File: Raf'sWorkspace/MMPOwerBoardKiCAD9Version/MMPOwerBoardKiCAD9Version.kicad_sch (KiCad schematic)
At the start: 31 parts, among them J1 TYPE-C-31-M-04, J2 Conn_02x16_Odd_Even, U1 HUSB237, U10 TPS22917DBVR, U2 TP4056-42-ESOP8, U3 DRV8833PWPR, U4 TPS63802DLAR, U5 TPS22917DBVR, U6 TPS61235PRWLR, U7 INA219AIDR, U8 TPS62133RGTR, U9 DRV8833PWPR

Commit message: Added a few things to schematic and added new LDO schematic to library
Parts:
- added C10, C11, C12, C14: 22u, symbol Device:C
- added C13, C8: 10u, symbol Device:C
- added C9: 1u, symbol Device:C
- added L1: 1uH, symbol Device:L
- added L2: 47uH, symbol Device:L
- added R12: 1M, symbol Device:R_Small_US
- added R13: 332k, symbol Device:R_Small_US
- added R14: 511k, symbol Device:R_Small_US
- added R15: 91k, symbol Device:R_Small_US
- added R16: 100k, symbol Device:R_Small_US
- added R17, R18: 4.7k, symbol Device:R_Small_US
- added U11: AMS1117-5.0, symbol AMS1117-CUSTOM5V:AMS1117-5.0
- U6: value TPS61235PRWLR -> TPS61236PRWLR
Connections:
- net 5V_OUT is gone; now on net 5V: J2.20 (Pin_20)
- net 3V3: now also U4.6 (VOUT), C14.1, R14.1
- net EXT_LOAD1_CTRL: now also U5.3 (ON), R17.1
- net EXT_LOAD1_OUT: now also U5.6 (VOUT)
- net EXT_LOAD2_CTRL: now also U10.3 (ON), R18.1
- net EXT_LOAD2_OUT: now also U10.6 (VOUT)
- net FromBattery: now also U4.1 (EN), U4.10 (VIN), U6.3 (VIN), U6.7 (EN), C13.1, C8.1, C9.1, L1.1, R16.1
- net GND: now also U10.2 (GND), U4.2 (MODE), U4.8 (GND), U5.2 (GND), U6.1 (PGND), C10.2, C11.2, C12.2, C13.2, C14.2, C8.2, C9.2, R17.2, R18.2
- net 5V: now reaches U5.1 (VIN)
- net 5V: now also U10.1 (VIN), U6.9 (VOUT), C10.1, C11.1, C12.1, R12.2
- net at U6.2 (SW): now also L1.2
- net GNDA: now reaches U6.4 (CC)
- net GNDA: now also U4.3 (AGND), U6.5 (AGND), U6.8 (INACT), R13.1, R15.2
- net at U6.6 (FB): now also R12.1, R13.2
- net at U4.4 (FB): now also R14.2, R15.1
- net at U4.5 (PG): now also R16.2
- net at U4.7 (L2): now also L2.1
- net at U4.9 (L1): now also L2.2
- no-connect marks 5 -> 9
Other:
- note added: "Make 0.whatever out of basic resistors"
- note added: "May wnat quick output discharge, only requires resistor but find out if worth it"
- note added: "STill need to get footprint from EASYEDA"
- moved on the sheet: C1, C2, C3, C4, C5, C6, C7, J1, R1, R10, R11, R2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

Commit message: Almost complete schematic
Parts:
- removed U8: TPS62133RGTR, TPS62133RGTR:QFN50P300X300X100-17N, symbol TPS62133RGTR:TPS62133RGTR
- added C15: 100n, symbol Device:C
- added C16: 1u, symbol Device:C
- added C18, C19: 22u, symbol Device:C
- added C20, C21: 10u, symbol Device:C
- added Q1: SS8050, Package_TO_SOT_SMD:SOT-23, symbol Transistor_BJT:SS8050
- added R19: 75k, symbol Device:R_Small_US
- added R20, R21, R22: 1M, symbol Device:R_Small_US
- added R23, R24: 1, symbol Device:R_Small_US
- added R25: 5.6k, symbol Device:R_Small_US
- added R26: 2.2k, symbol Device:R_Small_US
- added R27: 3.3k, symbol Device:R_Small_US
- U11: footprint (none) -> AMS1117_5.0_CUSTOM_FOOT:SOT-223_L6.5-W3.5-P2.30-LS7.0-BR
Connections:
- net HV is gone; now on net 9V: J2.22 (Pin_22)
- net 3V3: no longer C7.1, U7.1 (A1), U7.2 (A0), U7.5 (VS)
- net Battery: now also C7.1, U7.1 (A1), U7.2 (A0), U7.5 (VS)
- net ChargingCircuit: now also U2.5 (BAT), C21.1
- net FAST_CHARGE_CTRL: now also R27.1
- net FromBattery: no longer C13.1, C8.1, C9.1, L1.1, R16.1, U4.1 (EN), U4.10 (VIN), U6.3 (VIN), U6.7 (EN)
- net GND: now also J1.A1 (GND_A), J1.A12 (GND_A), J1.B1 (GND_B), J1.B12 (GND_B), U1.7 (GND), U11.1 (GND), U2.1 (TEMP), U2.3 (GND), U2.9 (EXP), C15.2, C16.2, C18.2, C19.2, C20.2, C21.2, Q1.2 (E), R19.2, R20.2, R21.2, R22.2, R25.1
- net LoadCircuit: now also C13.1, C8.1, C9.1, L1.1, R16.1, U4.1 (EN), U4.10 (VIN), U6.3 (VIN), U6.7 (EN)
- net at U11.2 (Vout): now also C19.1, R23.1, R24.1
- net 9V: now reaches U11.3 (Vin)
- net 9V: now also J1.A4 (VBUS_A), J1.A9 (VBUS_A), J1.B4 (VBUS_B), J1.B9 (VBUS_B), U1.2 (VUSB), C16.1, C18.1
- net at J1.A5 (CC1): now also U1.1 (CC1)
- net at J1.A6 (DP1): now also J1.B6 (DP2), U1.4 (D+)
- net at J1.A7 (DN1): now also J1.B7 (DN2), U1.5 (D-)
- net at J1.A8 (SUB1): now also R21.1
- net at J1.B5 (CC2): now also U1.6 (CC2)
- net at J1.B8 (SUB2): now also R22.1
- net at J1.S1 (SHIELD), J1.S2 (SHIELD), J1.S3 (SHIELD)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: now also C15.1, R20.1
- net at U2.2 (PROG): now also R25.2, R26.2
- net at U2.4 (VCC): now also U2.8 (CE), C20.1, R23.2, R24.2
- net at U1.3 (VSET): now also R19.1
- new net: Q1.3 (C), R26.1
- new net: Q1.1 (B), R27.2
- no-connect marks 9 -> 18
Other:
- note added: "Thermal Pad to GND, asks for via's, might be expensive... Current limiting ?"
- note removed: "STill need to get footprint from EASYEDA"
- note removed: "Thermal Pad to GND, asks for via's, might be expensive..."
- moved on the sheet: J1, U1, U11, U2

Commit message: Final Schematic complete with test points and jumpers
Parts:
- added D1, D2: LED, symbol Device:LED
- added JP1, JP2, JP3, JP4, JP5, JP6, JP7: SolderJumper_2_Open, symbol Jumper:SolderJumper_2_Open
- added L3: 22uH, symbol Device:L
- added R28, R29: 1k, symbol Device:R_Small_US
- added R30, R31, R32, R33: 0.1, symbol Device:R_Small_US
- added R34, R35, R37: 1, symbol Device:R_Small_US
- added R36: 2.2k, symbol Device:R_Small_US
- added TP1, TP10, TP11, TP12, TP13, TP14, TP15, TP16, TP17, TP18, TP19, TP2, TP3, TP4, TP5, TP6, TP7, TP8, TP9: TestPoint, symbol Connector:TestPoint
- L2: value 47uH -> 22uH
- R1, R2, R3, R4, R6, R7: footprint (none) -> Resistor_SMD:R_1206_3216Metric
- R13: value 332k -> 330k
- R14: value 511k -> 560k
- R15: value 91k -> 100k
- R5, R8: value 2 -> 1; footprint (none) -> Resistor_SMD:R_1206_3216Metric
- R9: value 0.4 -> 0.1
- SW1: footprint (none) -> SlideSwitch:SS-12D11-G050
- U1: footprint (none) -> HUSB237-AA001-DN06R:HUSB237-AA001DN06R-
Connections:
- net 3V3: now also C7.1, U7.1 (A1), U7.2 (A0), U7.5 (VS), JP2.2 (B); no longer C14.1, R14.1, U4.6 (VOUT)
- net 5V: now also JP3.1 (A); no longer C10.1, C11.1, C12.1, R12.2, U6.9 (VOUT)
- net 9V: now also JP1.1 (A); no longer C16.1, J1.A4 (VBUS_A), J1.A9 (VBUS_A), J1.B4 (VBUS_B), J1.B9 (VBUS_B), U1.2 (VUSB)
- net Battery: now also SW1.2; no longer C7.1, R9.1, U7.1 (A1), U7.2 (A0), U7.5 (VS), U7.8 (VIN+)
- net EXT_LOAD1_OUT: now also TP4.1
- net EXT_LOAD2_OUT: now also TP3.1
- net FromBattery: now also R9.1, SW1.3, U7.8 (VIN+), R30.1, R31.1, R32.1, R33.1, TP1.1; no longer R9.2, SW1.2, U7.7 (VIN-)
- net GND: now also JP5.2 (B), JP6.2 (B), TP14.1, TP18.1; no longer R3.2, R5.2, R6.2, R8.2
- net GNDA: now also TP10.1, TP9.1
- net LoadCircuit: now also R9.2, U7.7 (VIN-), R30.2, R31.2, R32.2, R33.2, TP2.1; no longer SW1.3
- net Motor2_A_OUT: now also TP6.1
- net Motor2_B_OUT: now also TP5.1
- net Motor4_A_OUT: now also TP16.1
- net Motor4_B_OUT: now also TP15.1
- net at R2.1, U3.3 (AISEN): now also JP6.1 (A)
- net at R1.1, U3.6 (BISEN): now also JP5.1 (A)
- net at R25.2, U2.2 (PROG): now also JP7.2 (B); no longer R26.2
- net at R3.1, R4.1, R5.1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: now also TP19.1
- net at R6.1, R7.1, R8.1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: now also TP17.1
- net at C19.1, U11.2 (Vout): now also JP4.1 (A); no longer R23.1, R24.1
- net at C20.1, R23.2, R24.2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: now also R37.2
- net at R12.1, U6.6 (FB): now also R36.2, TP8.1; no longer R13.2
- net at R14.2, R15.1, U4.4 (FB): now also C14.1, R14.1, R16.2, U4.5 (PG), U4.6 (VOUT), JP2.1 (A), TP11.1, TP12.1
- net at R19.1, U1.3 (VSET): now also TP13.1
- net at U4.7 (L2): now also L3.1; no longer L2.1
- net at U2.6 (~{STDBY}): now also R29.2
- net at U2.7 (~{CHRG}): now also R28.2
- new net: JP7.1 (A), R26.2
- new net: D1.1 (K), R29.1
- new net: C10.1, C11.1, C12.1, JP3.2 (B), R12.2, TP7.1, U6.9 (VOUT)
- new net: R34.1, R8.2
- new net: R34.2, R6.2
- new net: R13.2, R36.1
- new net: R35.1, R5.2
- new net: C16.1, J1.A4 (VBUS_A), J1.A9 (VBUS_A), J1.B4 (VBUS_B), J1.B9 (VBUS_B), JP1.2 (B), U1.2 (VUSB)
- new net: D2.1 (K), R28.1
- new net: R3.2, R35.2
- new net: L2.1, L3.2
- new net 5V_charge: D1.2 (A), D2.2 (A), JP4.2 (B), R23.1, R24.1, R37.1
- no-connect marks 18 -> 20
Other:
- moved on the sheet: C1, C10, C11, C12, C13, C14, C2, C20, C21, C3, C4, C5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

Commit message: Added BOM and PCB and LCSC numbers, Schematic complete
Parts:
- added FB1: FerriteBead_Small, FerriteBeadCustom:L0603, symbol Device:FerriteBead_Small
- added J3: Conn_01x02, Connector_JST:JST_PH_B2B-PH-K_1x02_P2.00mm_Vertical, symbol Connector_Generic:Conn_01x02
- C1, C6: footprint (none) -> Capacitor_SMD:C_0603_1608Metric; LCSC (none) -> C23630
- C10, C11, C12, C14, C18, C19: footprint (none) -> Capacitor_SMD:C_0603_1608Metric; LCSC (none) -> C59461
- C13, C2, C20, C21, C5, C8: footprint (none) -> Capacitor_SMD:C_0603_1608Metric; LCSC (none) -> C19702
- C15, C7: footprint (none) -> Capacitor_SMD:C_0603_1608Metric; LCSC (none) -> C14663
- C16, C9: footprint (none) -> Capacitor_SMD:C_0402_1005Metric; LCSC (none) -> C52923
- C3, C4: footprint (none) -> Capacitor_SMD:C_0805_2012Metric; LCSC (none) -> C1710
- D1, D2: footprint (none) -> LED_SMD:LED_0805_2012Metric; LCSC (none) -> C84256
- J1: LCSC (none) -> C129018
- J2: footprint (none) -> Connector_PinHeader_2.54mm:PinHeader_2x16_P2.54mm_Vertical; now left out of the parts list
- JP1, JP2, JP3, JP4, JP5, JP6, JP7: footprint (none) -> Jumper:SolderJumper-2_P1.3mm_Open_Pad1.0x1.5mm
- L1: footprint (none) -> Inductor_SMD:L_0805_2012Metric; LCSC (none) -> C1042
- L2, L3: value 22uH -> 220n; footprint (none) -> CustomInductor12.5x12.5mm:IND-SMD_L4.5-W4.1_TMPA0402SP; LCSC (none) -> C2875615
- Q1: LCSC (none) -> C2150
- R1, R2, R3, R4, R5, R6, R7, R8: LCSC (none) -> C17928
- R10, R11: footprint (none) -> Resistor_SMD:R_0805_2012Metric; LCSC (none) -> C26010
- R12, R20, R21, R22: footprint (none) -> Resistor_SMD:R_0603_1608Metric; LCSC (none) -> C22935
- R13: footprint (none) -> Resistor_SMD:R_0603_1608Metric_Pad0.98x0.95mm_HandSolder; LCSC (none) -> C23137
- R14: footprint (none) -> Resistor_SMD:R_0603_1608Metric_Pad0.98x0.95mm_HandSolder; LCSC (none) -> C23203
- R15, R16: footprint (none) -> Resistor_SMD:R_1206_3216Metric; LCSC (none) -> C17900
- R17, R18: footprint (none) -> Resistor_SMD:R_1206_3216Metric; LCSC (none) -> C17936
- R19: footprint (none) -> Resistor_SMD:R_0805_2012Metric_Pad1.20x1.40mm_HandSolder; LCSC (none) -> C17819
- R23, R24, R34, R35, R37: footprint (none) -> Resistor_SMD:R_1206_3216Metric; LCSC (none) -> C17928
- R25: footprint (none) -> Resistor_SMD:R_0805_2012Metric; LCSC (none) -> C4382
- R26: footprint (none) -> Resistor_SMD:R_0603_1608Metric_Pad0.98x0.95mm_HandSolder; LCSC (none) -> C4190
- R27: footprint (none) -> Resistor_SMD:R_0805_2012Metric_Pad1.20x1.40mm_HandSolder; LCSC (none) -> C26010
- R28, R29: footprint (none) -> Resistor_SMD:R_1206_3216Metric; LCSC (none) -> C4410
- R30, R31, R32, R33, R9: footprint (none) -> Resistor_SMD:R_1206_3216Metric; LCSC (none) -> C25334
- R36: footprint (none) -> Resistor_SMD:R_0603_1608Metric; LCSC (none) -> C4190
- SW1: value ~ -> SS-12D11-G050; LCSC (none) -> C17179528
- TP1, TP10, TP11, TP12, TP13, TP14, TP15, TP16, TP17, TP18, TP19, TP2, TP3, TP4, TP5, TP6, TP7, TP8, TP9: footprint (none) -> TestPoint:TestPoint_Pad_1.5x1.5mm; now left out of the parts list
- U1: LCSC (none) -> C22373734
- U10, U5: LCSC (none) -> C2681320
- U11: LCSC (none) -> C6187
- U2: LCSC (none) -> C16581
- U3, U9: LCSC (none) -> C50506
- U4: LCSC (none) -> C2845237
- U6: LCSC (none) -> C130295
- U7: LCSC (none) -> C138706
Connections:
- net Battery: now also J3.1 (Pin_1)
- net GND: now also FB1.2, J3.2 (Pin_2)
- net GNDA: now also FB1.1
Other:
- note added: "Get Footprint or something"
- moved on the sheet: C13, C14, C18, C19, C20, C21, D1, D2, JP2, JP4, JP7, L2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

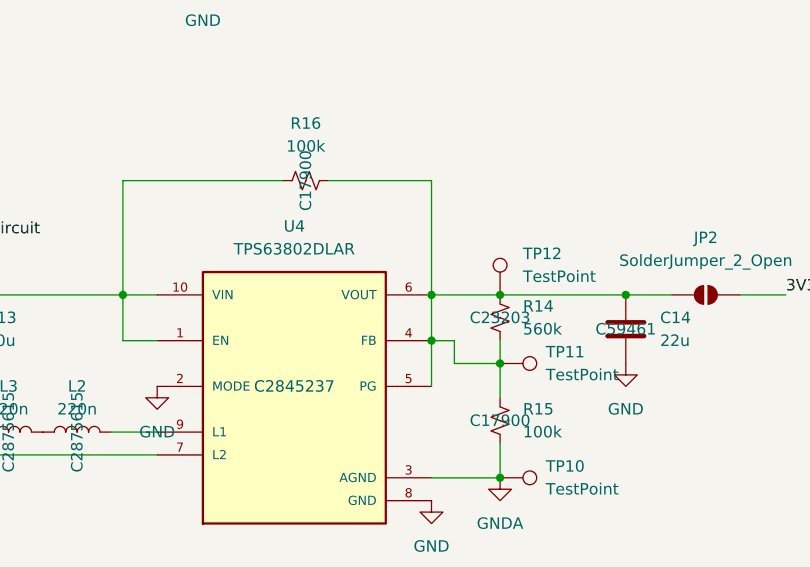
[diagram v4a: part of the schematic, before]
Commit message: Organised PCB on recommended board size
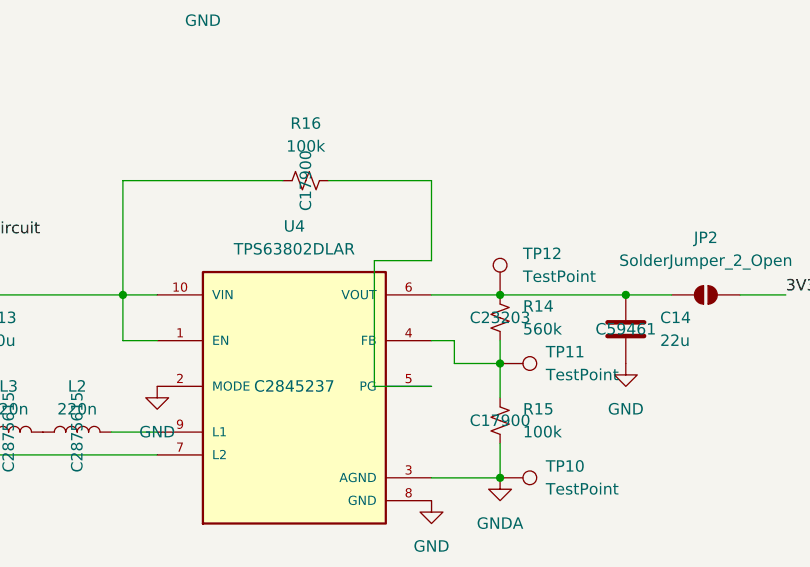
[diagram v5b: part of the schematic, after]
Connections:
- new net: C14.1, JP2.1 (A), R14.1, TP12.1, U4.6 (VOUT)
- new net: R14.2, R15.1, TP11.1, U4.4 (FB)
- new net: R16.2, U4.5 (PG)
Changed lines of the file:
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@@
-	)
-	(junction
-		(at 356.87 104.14)
-		(diameter 0)
-		(color 0 0 0 0)
 	)
 	(junction
@@
 	(junction
 		(at 24.13 135.89)
-		(diameter 0)
-		(color 0 0 0 0)
-	)
-	(junction
-		(at 356.87 99.06)
 		(diameter 0)
 		(color 0 0 0 0)
@@
 	(wire
 		(pts
+			(xy 356.87 95.25) (xy 356.87 86.36)
+		)
+		(stroke
+			(width 0)
+			(type default)
+		)
+	)
+	(wire
+		(pts
 			(xy 54.61 152.4) (xy 39.37 152.4)
 		)
@@
 	(wire
 		(pts
+			(xy 350.52 109.22) (xy 350.52 95.25)
+		)
+		(stroke
+			(width 0)
+			(type default)
+		)
+	)
+	(wire
+		(pts
 			(xy 361.95 31.75) (xy 356.87 31.75)
 		)
@@
 	(wire
 		(pts
+			(xy 356.87 109.22) (xy 350.52 109.22)
+		)
+		(stroke
+			(width 0)
+			(type default)
+		)
+	)
+	(wire
+		(pts
 			(xy 163.83 151.13) (xy 158.75 151.13)
 		)
@@
 	(wire
 		(pts
-			(xy 356.87 99.06) (xy 356.87 104.14)
-		)
-		(stroke
-			(width 0)
-			(type default)
-		)
-	)
-	(wire
-		(pts
 			(xy 144.78 35.56) (xy 152.4 35.56)
 		)
@@
 	(wire
 		(pts
-			(xy 356.87 86.36) (xy 356.87 99.06)
-		)
-		(stroke
-			(width 0)
-			(type default)
-		)
-	)
-	(wire
-		(pts
 			(xy 76.2 129.54) (xy 80.01 129.54)
 		)
@@
 	(wire
 		(pts
+			(xy 350.52 95.25) (xy 356.87 95.25)
+		)
+		(stroke
+			(width 0)
+			(type default)
+		)
+	)
+	(wire
+		(pts
 			(xy 121.92 40.64) (xy 129.54 40.64)
 		)
@@
 		)
 		(stroke
-			(width 0)
-			(type default)
-		)
-	)
-	(wire
-		(pts
-			(xy 356.87 104.14) (xy 356.87 109.22)
-		)
-		(stroke

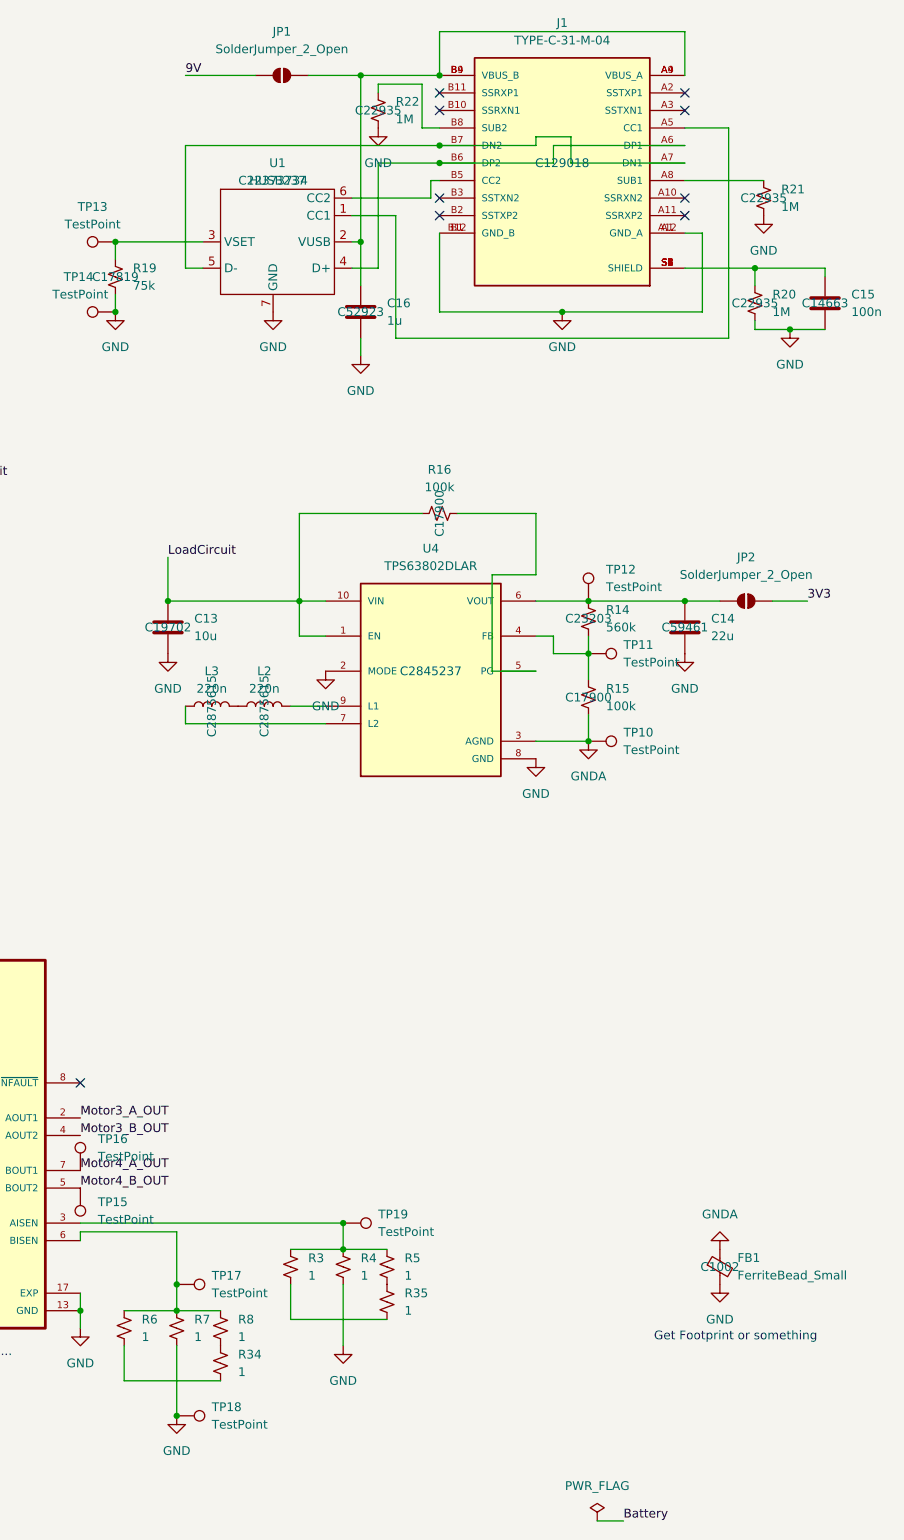
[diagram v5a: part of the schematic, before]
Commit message: Added all tracks
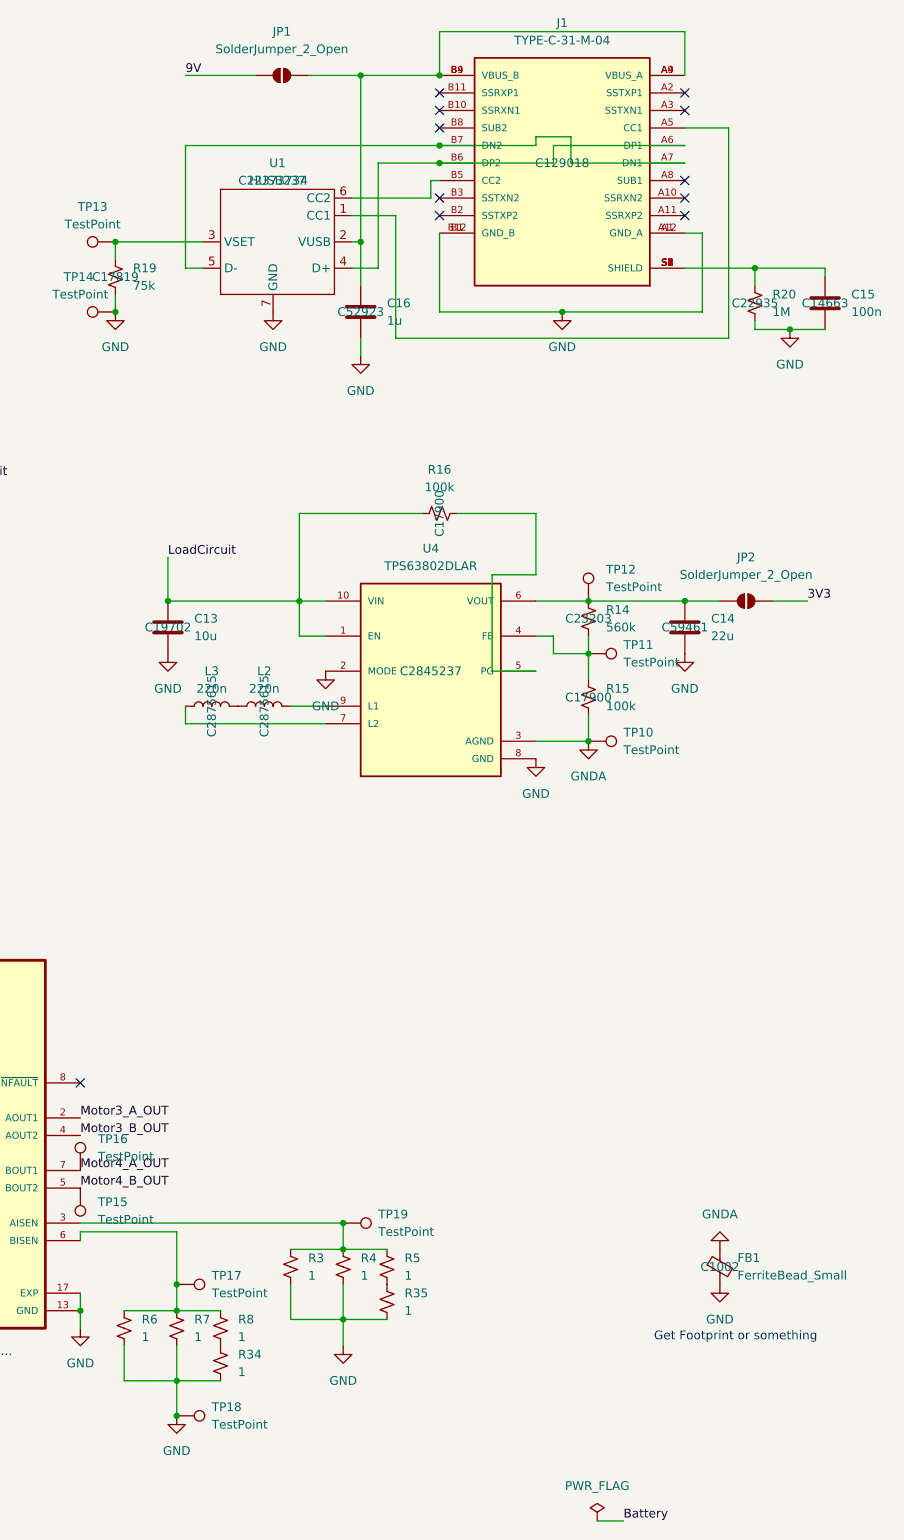
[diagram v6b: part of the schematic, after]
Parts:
- removed R21, R22: 1M, Resistor_SMD:R_0603_1608Metric, symbol Device:R_Small_US
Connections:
- net GND: now also R3.2, R34.2, R35.2, R6.2
- no-connect marks 20 -> 22
